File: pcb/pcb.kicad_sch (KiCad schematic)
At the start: 47 parts, among them J10 Conn_02x10_Counter_Clockwise, J11 Conn_01x03, J12 Conn_01x02, J13 Conn_01x06, J15 Conn_01x10, J16 Conn_01x10, J5 Conn_01x03, J6 Conn_01x03, J7 Conn_01x03, J8 Conn_01x03, J9 Conn_01x03, Q1 IRF9Z34NPBF, Q2 IRF9Z34NPBF, Q3 IRF9Z34NPBF, Q4 IRF9Z34NPBF, Q5 IRF9Z34NPBF, U1 ACS711ELCTR-12AB-T, U2 ACS711ELCTR-12AB-T, U3 ACS711ELCTR-12AB-T, U4 ACS711ELCTR-12AB-T, U5 ACS711ELCTR-12AB-T, U6 TXS0102DCUR, U7 TXS0102DCUR, U8 TXS0102DCUR

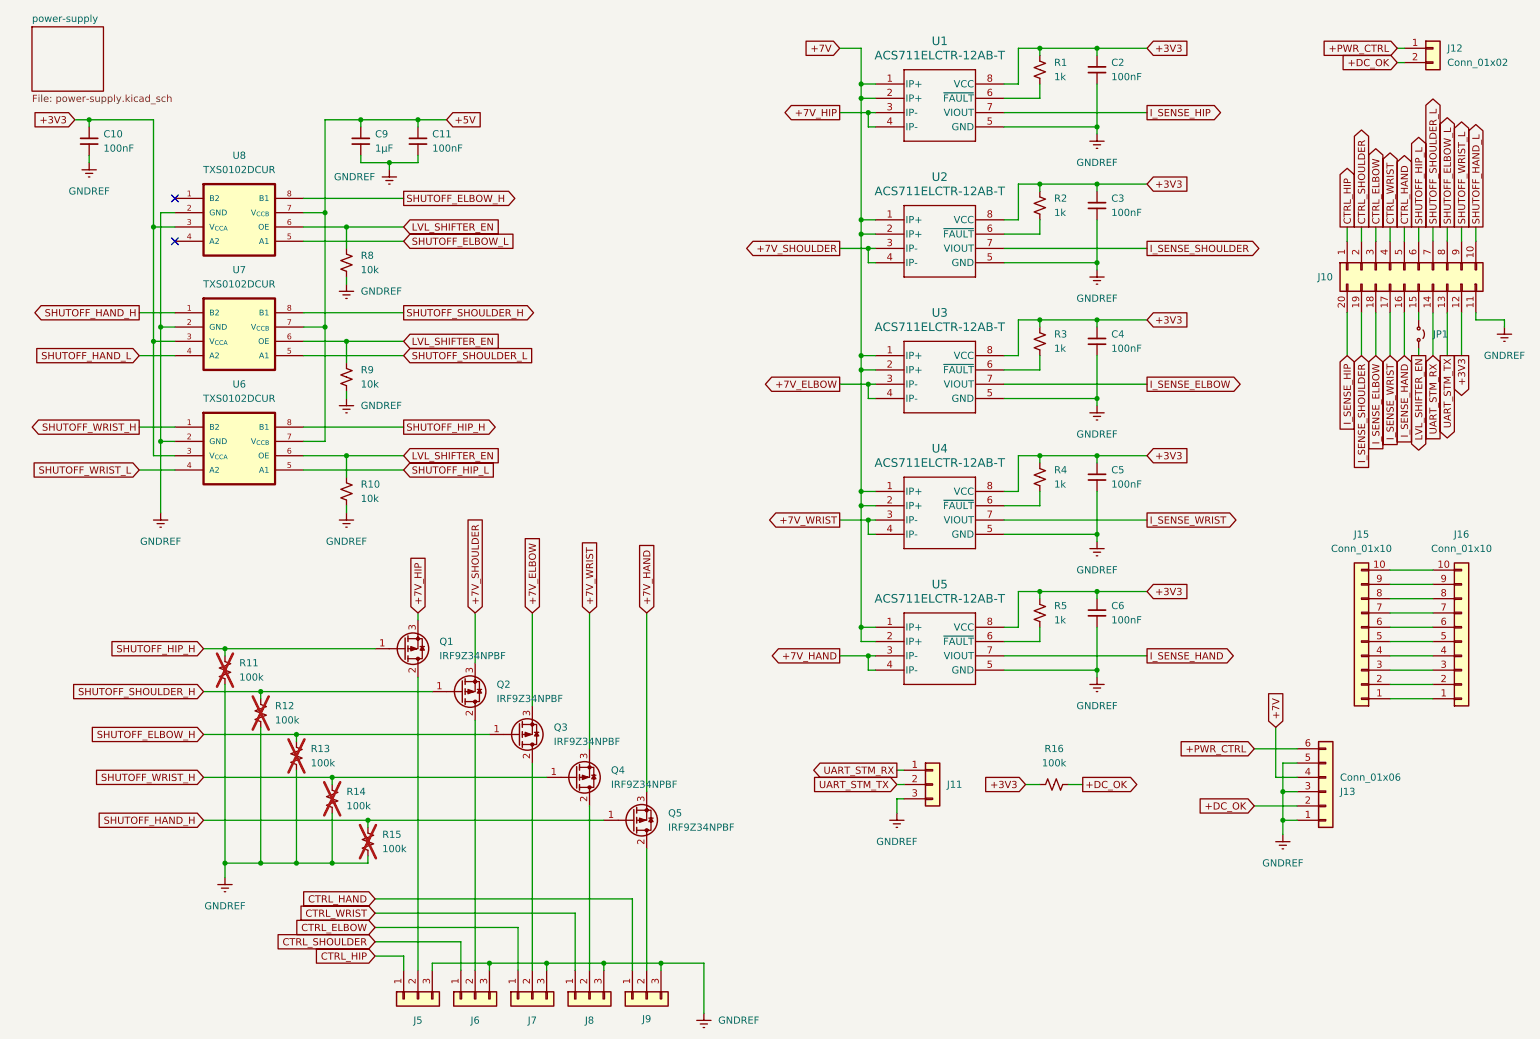
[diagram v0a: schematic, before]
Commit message: Swap servo label order for better layout
The schematic labels for the servo control and voltage signal nets were
previously assigned randomly. This commit reorders the labels so the two
larger servos are along the edge of the board for less interference on
adjacent Hall effect sensors. This commit also changes the labels so the
high side signals of each IC controls two MOSFETs that are close to each
other.
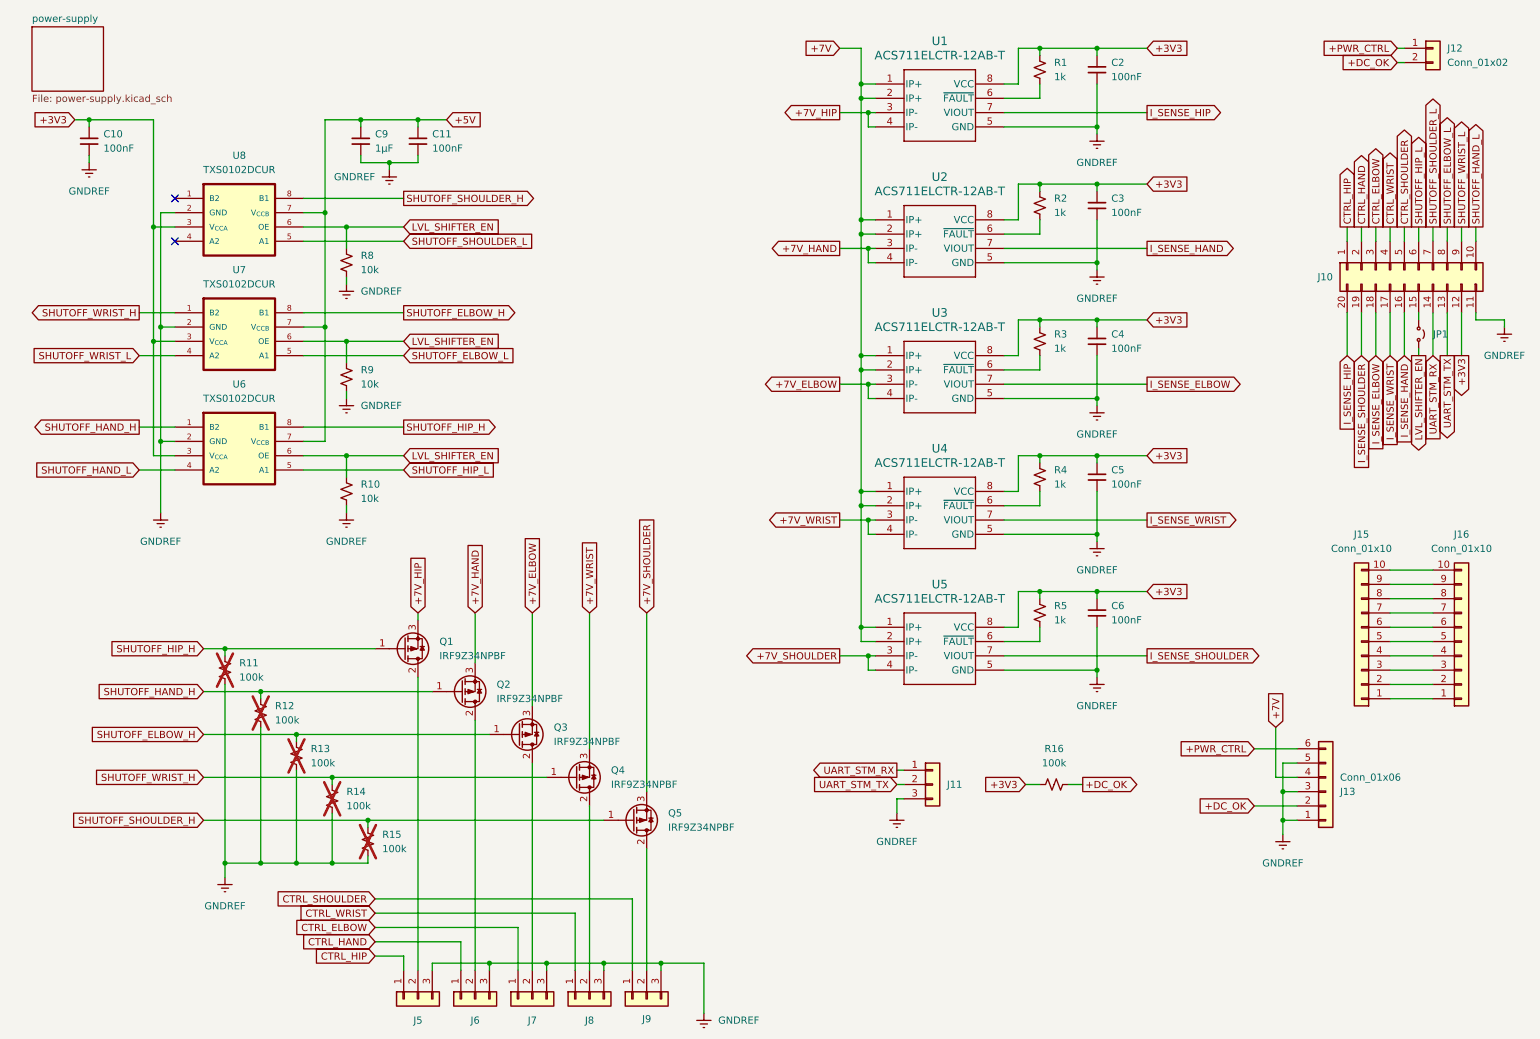
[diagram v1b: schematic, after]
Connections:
- net +7V_HAND: now also Q2.3 (S), U2.3 (IP-), U2.4 (IP-); no longer Q5.3 (S), U5.3 (IP-), U5.4 (IP-)
- net +7V_SHOULDER: now also Q5.3 (S), U5.3 (IP-), U5.4 (IP-); no longer Q2.3 (S), U2.3 (IP-), U2.4 (IP-)
- net CTRL_HAND: now also J10.2 (Pin_2), J6.1 (Pin_1); no longer J10.5 (Pin_5), J9.1 (Pin_1)
- net CTRL_SHOULDER: now also J10.5 (Pin_5), J9.1 (Pin_1); no longer J10.2 (Pin_2), J6.1 (Pin_1)
- net I_SENSE_HAND: now also U2.7 (VIOUT); no longer U5.7 (VIOUT)
- net I_SENSE_SHOULDER: now also U5.7 (VIOUT); no longer U2.7 (VIOUT)
- net SHUTOFF_ELBOW_H: now also U7.8 (B1); no longer U8.8 (B1)
- net SHUTOFF_ELBOW_L: now also U7.5 (A1); no longer U8.5 (A1)
- net SHUTOFF_HAND_H: now also Q2.1 (G), R12.1, U6.1 (B2); no longer Q5.1 (G), R15.1, U7.1 (B2)
- net SHUTOFF_HAND_L: now also U6.4 (A2); no longer U7.4 (A2)
- net SHUTOFF_SHOULDER_H: now also Q5.1 (G), R15.1, U8.8 (B1); no longer Q2.1 (G), R12.1, U7.8 (B1)
- net SHUTOFF_SHOULDER_L: now also U8.5 (A1); no longer U7.5 (A1)
- net SHUTOFF_WRIST_H: now also U7.1 (B2); no longer U6.1 (B2)
- net SHUTOFF_WRIST_L: now also U7.4 (A2); no longer U6.4 (A2)

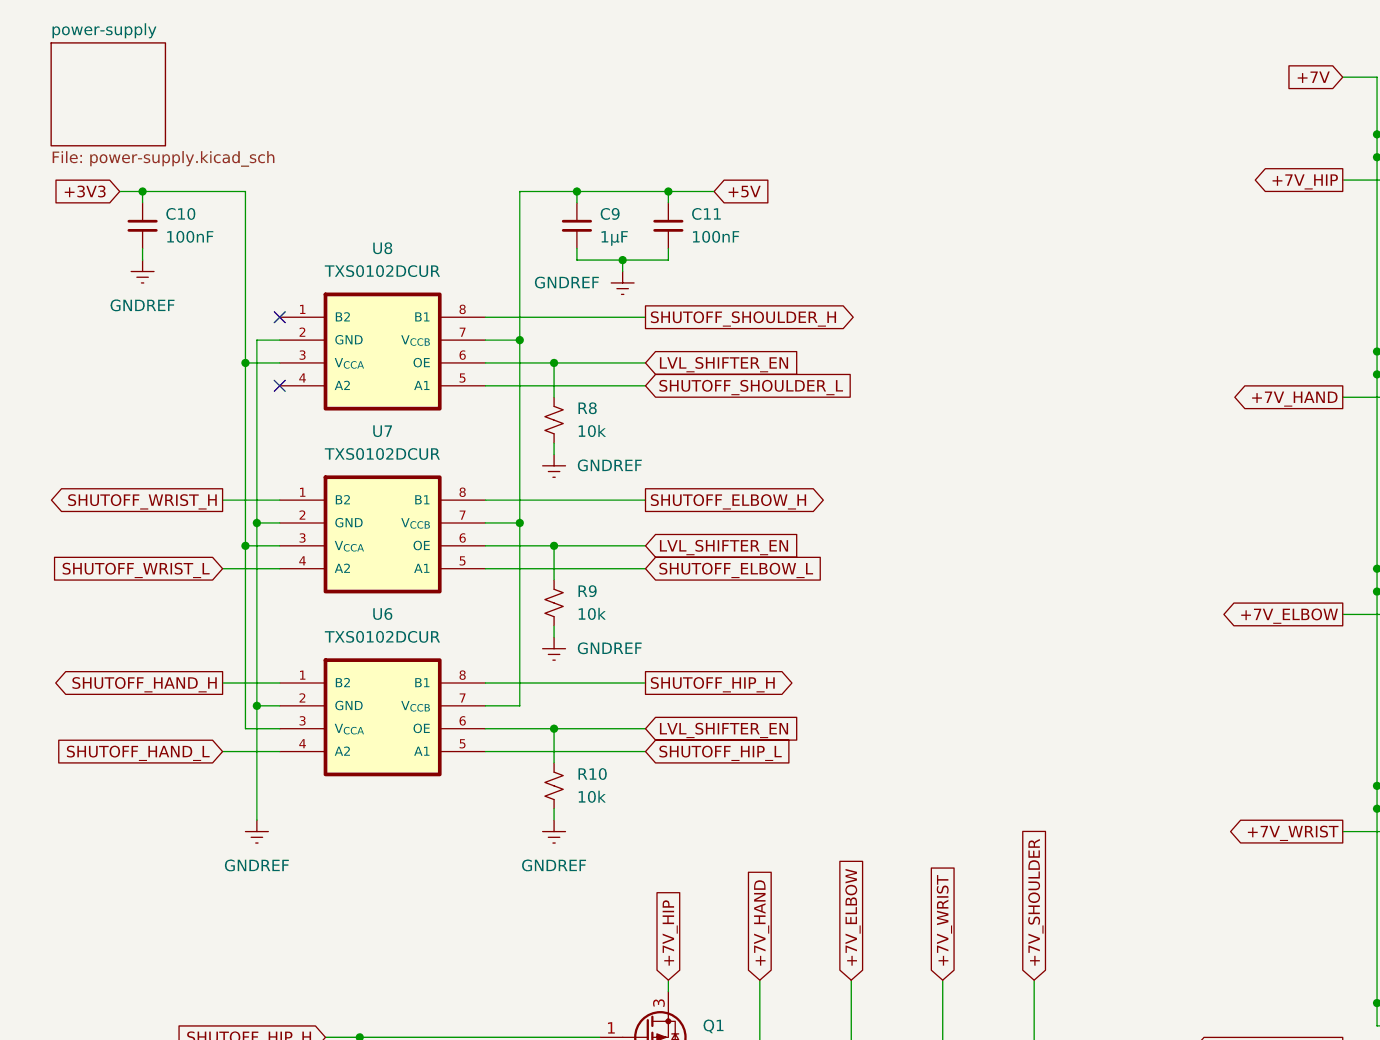
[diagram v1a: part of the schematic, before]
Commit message: Add bypass capacitors for each level shifter
The datasheet for the level shifter recommends placing the bypass
capacitors as close as possible to the IC. Ideally, we could probably
get away with just the one set. However, since the level shifters are
placed so far away from each other, it's probably better to have more
caps and slightly higher capacicance.
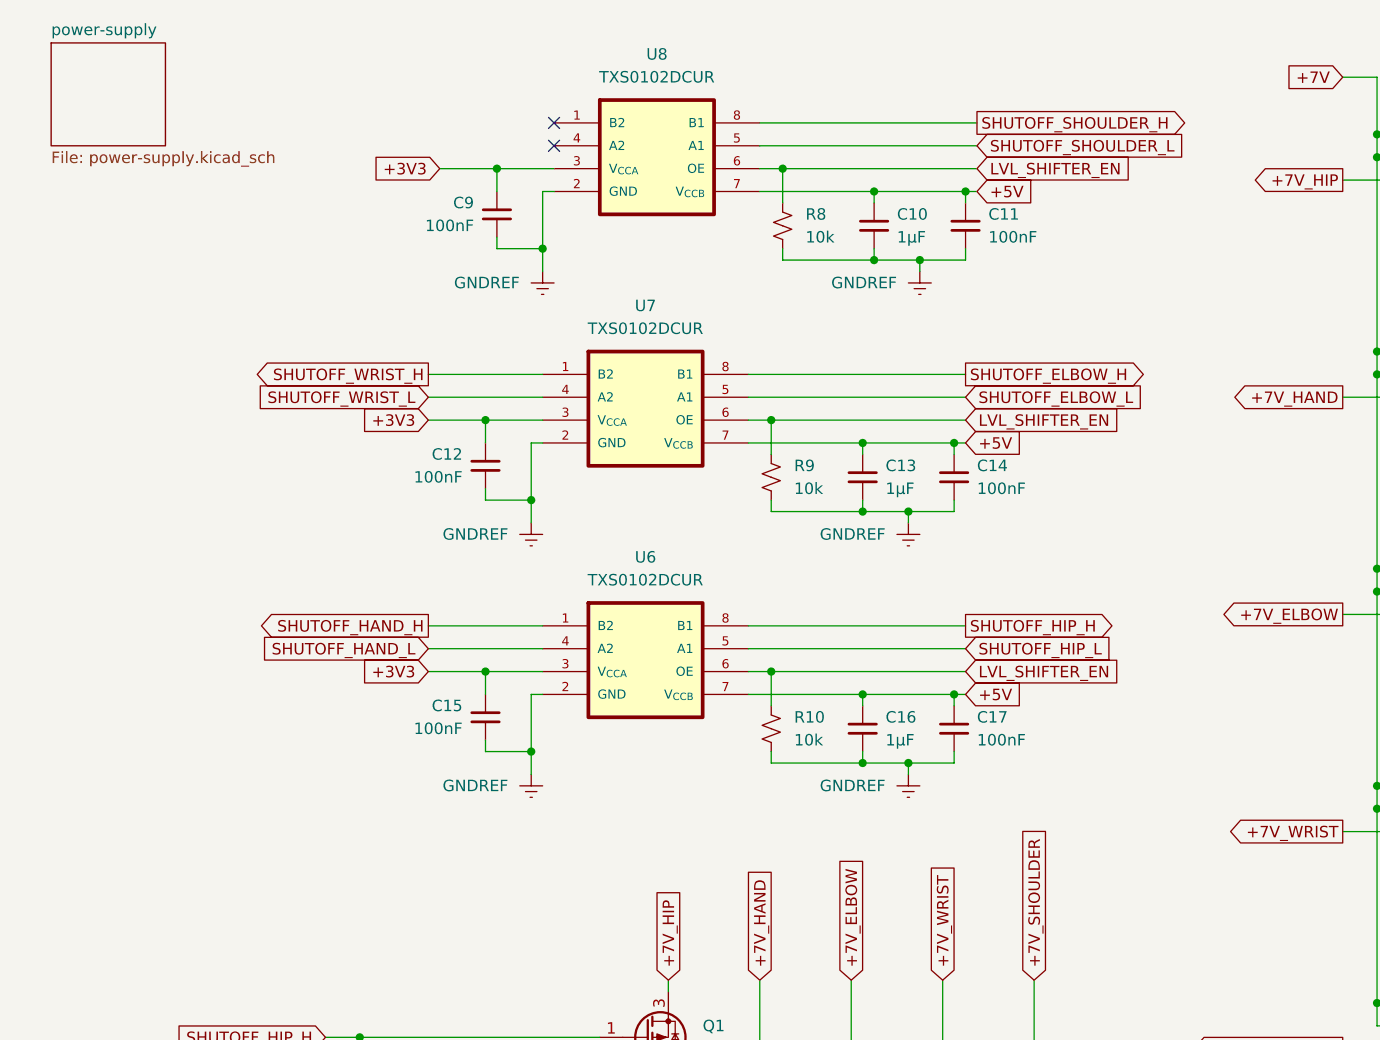
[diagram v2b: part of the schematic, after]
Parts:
- added C12, C14, C15, C17: 100nF, Capacitor_SMD:C_0805_2012Metric_Pad1.18x1.45mm_HandSolder, symbol Device:C_Small
- added C13, C16: 1µF, Capacitor_SMD:C_0805_2012Metric_Pad1.18x1.45mm_HandSolder, symbol Device:C_Small
- C10: value 100nF -> 1µF
- C9: value 1µF -> 100nF
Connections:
- net +3V3: now also C9.1, C12.1, C15.1; no longer C10.1
- net +5V: now also C10.1, C13.1, C14.1, C16.1, C17.1; no longer C9.1
- net GNDREF: now also C12.2, C13.2, C14.2, C15.2, C16.2, C17.2
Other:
- moved on the sheet: U6, U7, U8
